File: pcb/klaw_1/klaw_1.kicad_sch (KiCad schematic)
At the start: 71 parts, among them J1 PJ-320A-4P, J3 lv27, SW1 SW_PUSH-MX_W_LED, SW10 SW_PUSH-MX_W_LED, SW12 SW_PUSH-MX_W_LED, SW13 SW_PUSH-MX_W_LED, SW14 SW_PUSH-MX_W_LED, SW15 SW_PUSH-MX_W_LED, SW16 SW_PUSH-MX_W_LED, SW18 EC11E15244G1, SW2 SW_PUSH-MX_W_LED, SW20 SW_PUSH-MX_W_LED, SW21 SW_PUSH-MX_W_LED, SW3 SW_PUSH-MX_W_LED, SW4 SW_PUSH-MX_W_LED, SW5 SW_PUSH-MX_W_LED, SW6 SW_PUSH-MX_W_LED, SW7 SW_PUSH-MX_W_LED, SW8 SW_PUSH-MX_W_LED, SW9 SW_PUSH-MX_W_LED, U1 ProMicro

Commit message: feat: rev 2 - machine-assemblable LEDs (SK6812MINI-EA)
- LED footprint reworked for SK6812MINI-EA: 3.8x3.4 window per
  datasheet, EA land pattern, per-face pin maps chosen to preserve
  LED chain routing (F side rotated 180)
- LED chain start jumper JP26 removed; LED net routed directly
- sourcing swapped to C5378731 with MPN fields; LEDs marked as
  JLC-assembled, sockets remain hand-solder
- fab refresh: rev-2 gerbers, LED placement rows in both CPLs
  (41 placements/side), READMEs updated
- new EA 3D model
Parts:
- removed JP26: Device_Jumper_NO_Small, KLOR:Jumper, symbol KLORlib:Device_Jumper_NO_Small
- SW1, SW10, SW12, SW13, SW14, SW15, SW16, SW2, SW20, SW21, SW3, SW4, SW5, SW6, SW7, SW8, SW9: Assembly Hand-solder -> JLC; Checked 2026-08-20 -> 2026-08-21; LCSC C2886570 -> C5378731; MPN (none) -> SK6812MINI-EA; Price 0.0972@5 -> 0.0977@5; Socket_Assembly (none) -> Hand-solder; Stock 37840 -> 16625
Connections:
- net LED: now also SW20.3 (DIN)

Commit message: fix: encoder removed from assembly files
- EC11 knob must face the keycap side (opposite the component face),
  so machine-placing it with the belly-side parts was wrong on both
  CPLs; it is now a hand-solder part inserted from the keycap side
- assembly is 7 BOM lines / 40 placements per board, single-sided
- fab README documents build orientation: populated face is the
  keyboard underside; JLC preview showing Bottom-only for the left
  order is correct
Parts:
- SW18: Assembly JLC -> Hand-solder
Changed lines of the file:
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@@
 			)
 		)
-		(property "Assembly" "JLC"
+		(property "Assembly" "Hand-solder"
 			(at 46.99 180.594 0)
 			(hide yes)

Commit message: feat: wired-first config - PSW1 and BT1 DNP
- power switch and JST battery connector marked DNP in schematic
- removed from both assembly BOMs/CPLs (5 lines, 38 placements)
- build BOMs note the wired-config DNP
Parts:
- BT1, PSW1: now not fitted
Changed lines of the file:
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@@
 		(on_board yes)
 		(in_pos_files yes)
-		(dnp no)
+		(dnp yes)
 		(fields_autoplaced yes)
 		(property "Reference" "PSW1"
@@
 		(on_board yes)
 		(in_pos_files yes)
-		(dnp no)
+		(dnp yes)
 		(property "Reference" "BT1"
 			(at 92.202 174.244 0)

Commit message: fix: assembly files match confirmed KLOR mounting map
- right build keycap side = PCB front, so machine assembly runs on
  the Bottom layer for right halves and Top for left (was inverted)
- assembly reduced to component-face parts only: diodes + LEDs,
  2 BOM lines / 35 placements per side
- TRRS, buzzer, reset join encoder as keycap-face hand-solder parts
- per-side build BOMs rewritten with per-row mount faces
- fab README documents orientation and silkscreen viewer convention
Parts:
- BZ1, J1, RSW1: Assembly JLC -> Hand-solder
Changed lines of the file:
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@@
 			)
 		)
-		(property "Assembly" "JLC"
+		(property "Assembly" "Hand-solder"
 			(at 81.788 102.108 0)
 			(hide yes)
@@
 			)
 		)
-		(property "Assembly" "JLC"
+		(property "Assembly" "Hand-solder"
 			(at 111.76 39.624 0)
 			(hide yes)
@@
 			)
 		)
-		(property "Assembly" "JLC"
+		(property "Assembly" "Hand-solder"
 			(at 40.132 105.664 0)
 			(hide yes)

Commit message: feat: full JLC assembly - double-sided orders
- JLC assembles everything except DNP parts (PSW1, BT1) and
  user-supplied MCU/OLED; no soldering needed after assembly
- CPLs are double-sided: component face gets diodes, LEDs, and
  hotswap sockets (synthetic HSx rows); keycap face gets TRRS,
  buzzer, reset switch, encoder — 7 BOM lines, 56 placements/side
- Assembly fields and docs updated to match
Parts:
- BZ1, J1, RSW1, SW18: Assembly Hand-solder -> JLC
- SW1, SW10, SW12, SW13, SW14, SW15, SW16, SW2, SW20, SW21, SW3, SW4, SW5, SW6, SW7, SW8, SW9: Socket_Assembly Hand-solder -> JLC
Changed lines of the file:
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@@
 			)
 		)
-		(property "Socket_Assembly" "Hand-solder"
+		(property "Socket_Assembly" "JLC"
 			(at 196.596 123.952 0)
 			(hide yes)
@@
 			)
 		)
-		(property "Socket_Assembly" "Hand-solder"
+		(property "Socket_Assembly" "JLC"
 			(at 196.342 146.304 0)
 			(hide yes)
@@
 			)
 		)
-		(property "Assembly" "Hand-solder"
+		(property "Assembly" "JLC"
 			(at 81.788 102.108 0)
 			(hide yes)
@@
 			)
 		)
-		(property "Socket_Assembly" "Hand-solder"
+		(property "Socket_Assembly" "JLC"
 			(at 211.328 67.056 0)
 			(hide yes)
@@
 			)
 		)
-		(property "Socket_Assembly" "Hand-solder"
+		(property "Socket_Assembly" "JLC"
 			(at 193.548 67.056 0)
 			(hide yes)
@@
 			)
 		)
-		(property "Socket_Assembly" "Hand-solder"
+		(property "Socket_Assembly" "JLC"
 			(at 235.966 123.952 0)
 			(hide yes)
@@
 			)
 		)
-		(property "Socket_Assembly" "Hand-solder"
+		(property "Socket_Assembly" "JLC"
 			(at 211.328 39.116 0)
 			(hide yes)
@@
 			)
 		)
-		(property "Socket_Assembly" "Hand-solder"
+		(property "Socket_Assembly" "JLC"
 			(at 246.888 67.056 0)
 			(hide yes)
@@
 			)
 		)
-		(property "Assembly" "Hand-solder"
+		(property "Assembly" "JLC"
 			(at 111.76 39.624 0)
 			(hide yes)
@@
 			)
 		)
-		(property "Socket_Assembly" "Hand-solder"
+		(property "Socket_Assembly" "JLC"
 			(at 222.504 123.952 0)
 			(hide yes)
@@
 			)
 		)
-		(property "Socket_Assembly" "Hand-solder"
+		(property "Socket_Assembly" "JLC"
 			(at 229.108 67.056 0)
 			(hide yes)
@@
 			)
 		)
-		(property "Socket_Assembly" "Hand-solder"
+		(property "Socket_Assembly" "JLC"
 			(at 182.88 146.304 0)
 			(hide yes)
@@
 			)
 		)
-		(property "Assembly" "Hand-solder"
+		(property "Assembly" "JLC"
 			(at 40.132 105.664 0)
 			(hide yes)
@@
 			)
 		)
-		(property "Socket_Assembly" "Hand-solder"
+		(property "Socket_Assembly" "JLC"
 			(at 222.504 135.128 0)
 			(hide yes)
@@
 			)
 		)
-		(property "Socket_Assembly" "Hand-solder"
+		(property "Socket_Assembly" "JLC"
 			(at 175.768 53.086 0)
 			(hide yes)
@@
 			)
 		)
-		(property "Socket_Assembly" "Hand-solder"
+		(property "Socket_Assembly" "JLC"
 			(at 222.25 112.776 0)
 			(hide yes)
@@
 			)
 		)
-		(property "Socket_Assembly" "Hand-solder"
+		(property "Socket_Assembly" "JLC"
 			(at 248.92 112.776 0)
 			(hide yes)
@@
 			)
 		)
-		(property "Socket_Assembly" "Hand-solder"
+		(property "Socket_Assembly" "JLC"
 			(at 235.712 112.776 0)
 			(hide yes)
@@
 			)
 		)
-		(property "Assembly" "Hand-solder"
+		(property "Assembly" "JLC"
 			(at 46.99 180.594 0)
 			(hide yes)
@@
 			)
 		)
-		(property "Socket_Assembly" "Hand-solder"
+		(property "Socket_Assembly" "JLC"
 			(at 209.55 123.952 0)
 			(hide yes)
@@
 			)
 		)
-		(property "Socket_Assembly" "Hand-solder"
+		(property "Socket_Assembly" "JLC"
 			(at 193.548 53.086 0)
 			(hide yes)
@@
 			)
 		)
-		(property "Socket_Assembly" "Hand-solder"
+		(property "Socket_Assembly" "JLC"
 			(at 229.108 81.026 0)
 			(hide yes)
@@
 			)
 		)
-		(property "Socket_Assembly" "Hand-solder"
+		(property "Socket_Assembly" "JLC"
 			(at 235.966 135.128 0)
 			(hide yes)
@@
 			)
 		)
-		(property "Socket_Assembly" "Hand-solder"
+		(property "Socket_Assembly" "JLC"
 			(at 229.108 53.086 0)
 			(hide yes)
@@
 			)
 		)
-		(property "Socket_Assembly" "Hand-solder"
+		(property "Socket_Assembly" "JLC"
 			(at 246.888 53.086 0)
 			(hide yes)
@@
 			)
 		)
-		(property "Socket_Assembly" "Hand-solder"
+		(property "Socket_Assembly" "JLC"
 			(at 209.296 112.776 0)
 			(hide yes)
@@
 			)
 		)
-		(property "Socket_Assembly" "Hand-solder"
+		(property "Socket_Assembly" "JLC"
 			(at 193.548 39.116 0)
 			(hide yes)
@@
 			)
 		)
-		(property "Socket_Assembly" "Hand-solder"
+		(property "Socket_Assembly" "JLC"
 			(at 175.768 39.116 0)
 			(hide yes)
@@
 			)
 		)
-		(property "Socket_Assembly" "Hand-solder"
+		(property "Socket_Assembly" "JLC"
 			(at 246.888 39.116 0)
 			(hide yes)
@@
 			)
 		)
-		(property "Socket_Assembly" "Hand-solder"
+		(property "Socket_Assembly" "JLC"
 			(at 249.174 123.952 0)
 			(hide yes)
@@
 			)
 		)
-		(property "Socket_Assembly" "Hand-solder"
+		(property "Socket_Assembly" "JLC"
 			(at 196.342 112.776 0)
 			(hide yes)
@@
 			)
 		)
-		(property "Socket_Assembly" "Hand-solder"
+		(property "Socket_Assembly" "JLC"
 			(at 209.55 135.128 0)
 			(hide yes)
@@
 			)
 		)
-		(property "Socket_Assembly" "Hand-solder"
+		(property "Socket_Assembly" "JLC"
 			(at 175.768 67.056 0)
 			(hide yes)
@@
 			)
 		)
-		(property "Socket_Assembly" "Hand-solder"
+		(property "Socket_Assembly" "JLC"
 			(at 211.328 81.026 0)
 			(hide yes)
@@
 			)
 		)
-		(property "Socket_Assembly" "Hand-solder"
+		(property "Socket_Assembly" "JLC"
 			(at 249.174 135.128 0)
 			(hide yes)
@@
 			)
 		)
-		(property "Socket_Assembly" "Hand-solder"
+		(property "Socket_Assembly" "JLC"
 			(at 196.596 135.128 0)
 			(hide yes)
@@
 			)
 		)
-		(property "Socket_Assembly" "Hand-solder"
+		(property "Socket_Assembly" "JLC"
 			(at 211.328 53.086 0)
 			(hide yes)
@@
 			)
 		)
-		(property "Socket_Assembly" "Hand-solder"
+		(property "Socket_Assembly" "JLC"
 			(at 229.108 39.116 0)
 			(hide yes)

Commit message: feat: configuration jumpers become 0R resistors
- JP1-8 (OLED), JP16-21 (trackball), JP22-25 (JST polarity) now
  0R 0603 resistors (C21189, JLC Basic) placed per side by assembly
  instead of hand-bridged solder jumpers
- new R_0R schematic symbol, pin-compatible with the jumper symbol
- JST polarity pairs are face-exclusive (F: JP22+JP24, B: JP23+JP25)
  so per-side placement is polarity-correct by construction
- R_0603 footprint + 3D model added to project library
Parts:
- JP1, JP16, JP17, JP18, JP19, JP2, JP20, JP21, JP22, JP23, JP24, JP25, JP3, JP4, JP5, JP6, JP7, JP8: value Device_Jumper_NO_Small -> 0R; footprint KLOR:Jumper -> KLOR:R_0603_1608Metric; symbol KLORlib:Device_Jumper_NO_Small -> KLORlib:R_0R; Assembly (none) -> JLC; Checked (none) -> 2026-08-21; LCSC (none) -> C21189; MPN (none) -> 0603WAF0000T5E; Price (none) -> 0.004@100; Stock (none) -> 15480500

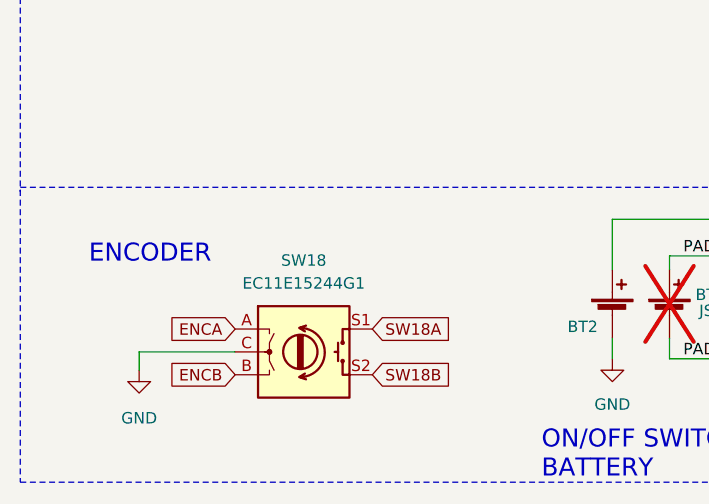
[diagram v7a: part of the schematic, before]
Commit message: feat: shorter encoder - Alps EC11N1525404
- replaces EC11E15244G1: same exact EC11 footprint, 15mm D-cut
  shaft, 19.5mm above PCB (was 24.5mm) - matches the original KLOR
  height spec; 30 det/15 pulse, 1.5mm switch travel
- official Alps 3D CAD model, baked to footprint orientation
- sourcing fields, build BOMs, and fab BOMs updated (C470748)
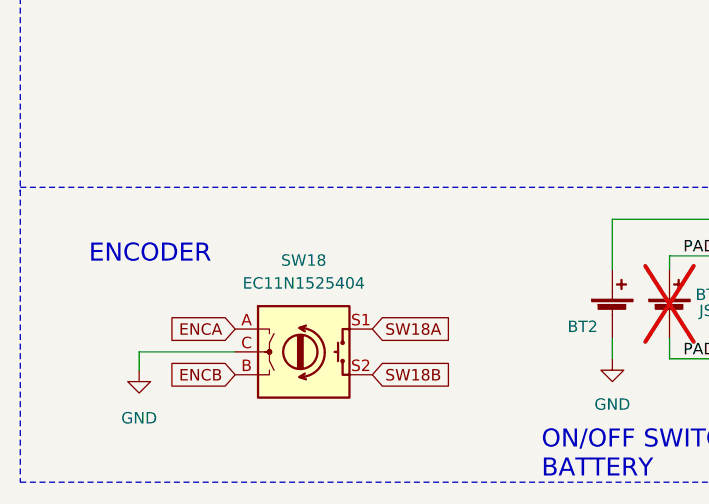
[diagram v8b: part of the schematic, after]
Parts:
- SW18: value EC11E15244G1 -> EC11N1525404; Checked 2026-08-20 -> 2026-08-22; LCSC C370970 -> C470748; MPN (none) -> EC11N1525404; Price 2.27@1 -> 2.77@1; Stock 1775 -> 2310
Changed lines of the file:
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@@
 			)
 		)
-		(property "Value" "EC11E15244G1"
+		(property "Value" "EC11N1525404"
 			(at 46.99 172.974 0)
 			(show_name no)
@@
 			)
 		)
-		(property "Datasheet" ""
+		(property "Datasheet" "https://www.lcsc.com/product-detail/C470748.html"
 			(at 46.99 173.99 0)
 			(hide yes)
@@
 			)
 		)
-		(property "LCSC" "C370970"
+		(property "LCSC" "C470748"
 			(at 46.99 180.594 0)
 			(hide yes)
@@
 			)
 		)
-		(property "Price" "2.27@1"
+		(property "Price" "2.77@1"
 			(at 46.99 180.594 0)
 			(hide yes)
@@
 			)
 		)
-		(property "Stock" "1775"
+		(property "Stock" "2310"
 			(at 46.99 180.594 0)
 			(hide yes)
@@
 			)
 		)
-		(property "Checked" "2026-08-20"
+		(property "Checked" "2026-08-22"
 			(at 46.99 180.594 0)
 			(hide yes)
@@
 			(at 46.99 180.594 0)
 			(hide yes)
+			(show_name no)
+			(do_not_autoplace no)
+			(effects
+				(font
+					(size 1.27 1.27)
+				)
+			)
+		)
+		(property "MPN" "EC11N1525404"
+			(at 46.99 180.594 0)
+			(hide yes)
